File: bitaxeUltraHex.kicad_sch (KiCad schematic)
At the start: 2 parts, among them J1 Conn_01x01, J2 Conn_01x01

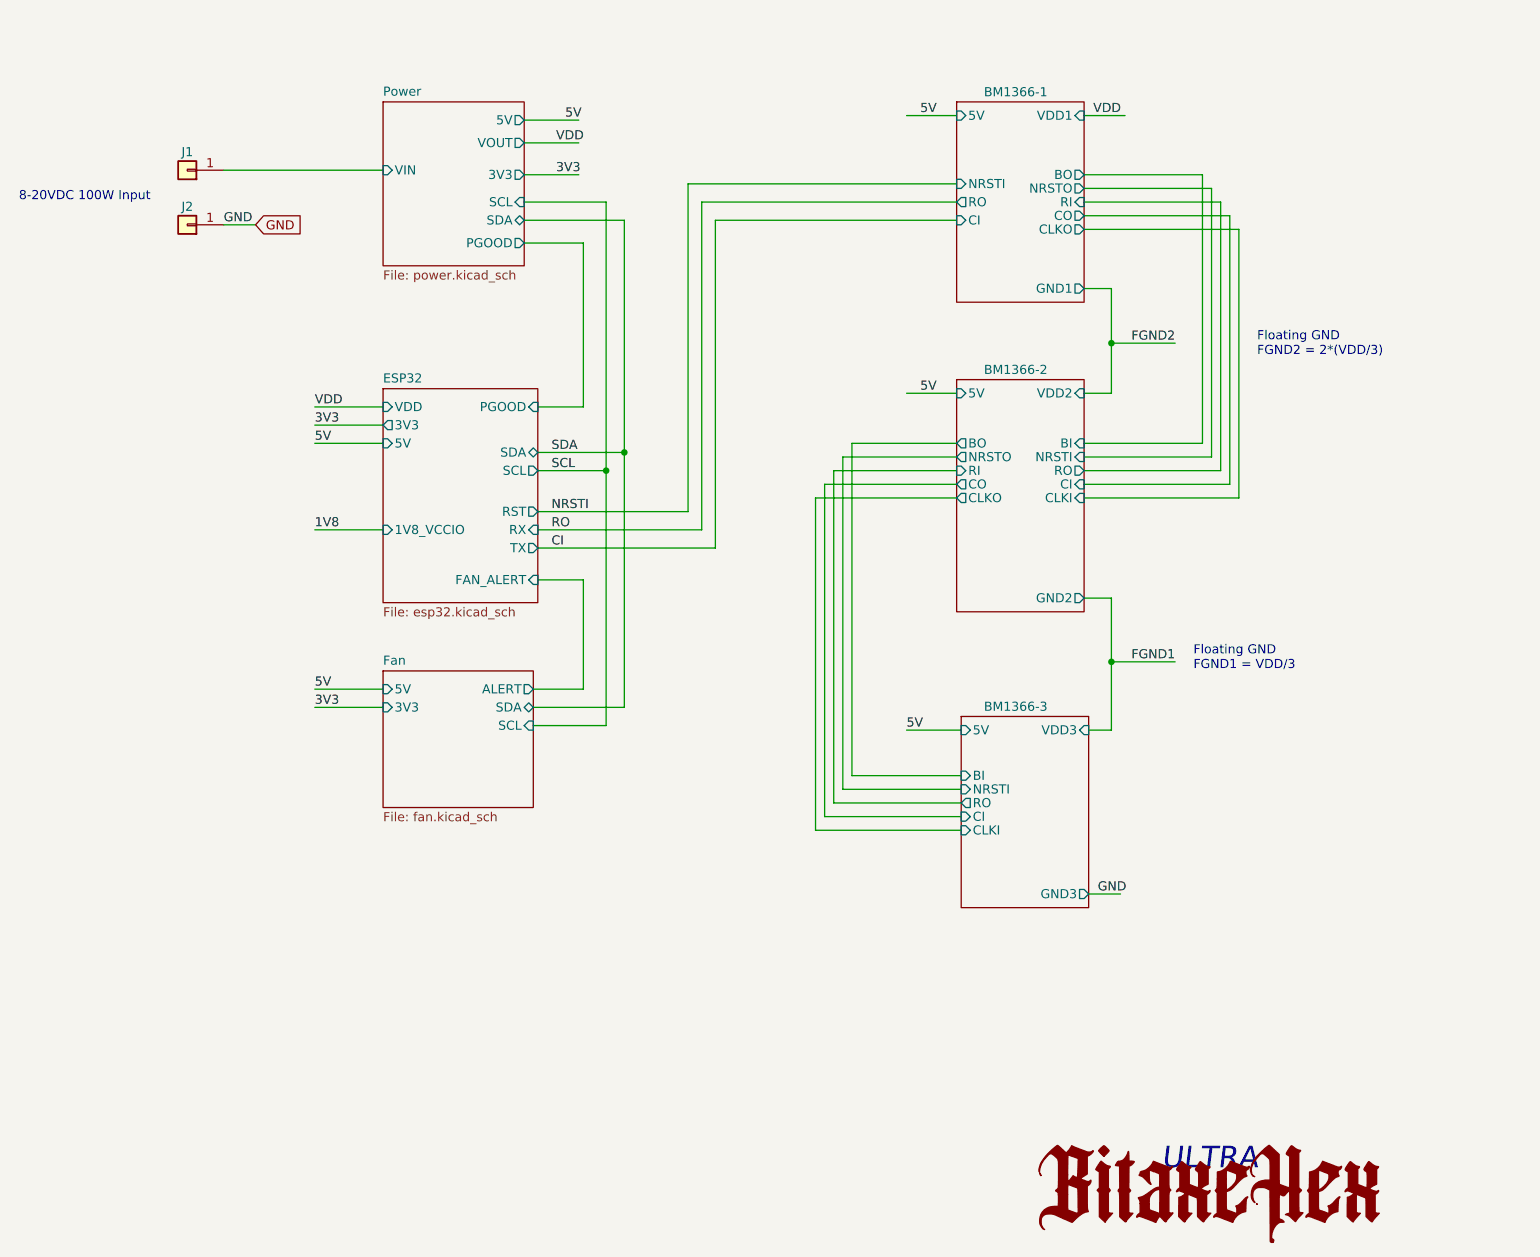
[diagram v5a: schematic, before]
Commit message: add level translator circuits to ASIC communications
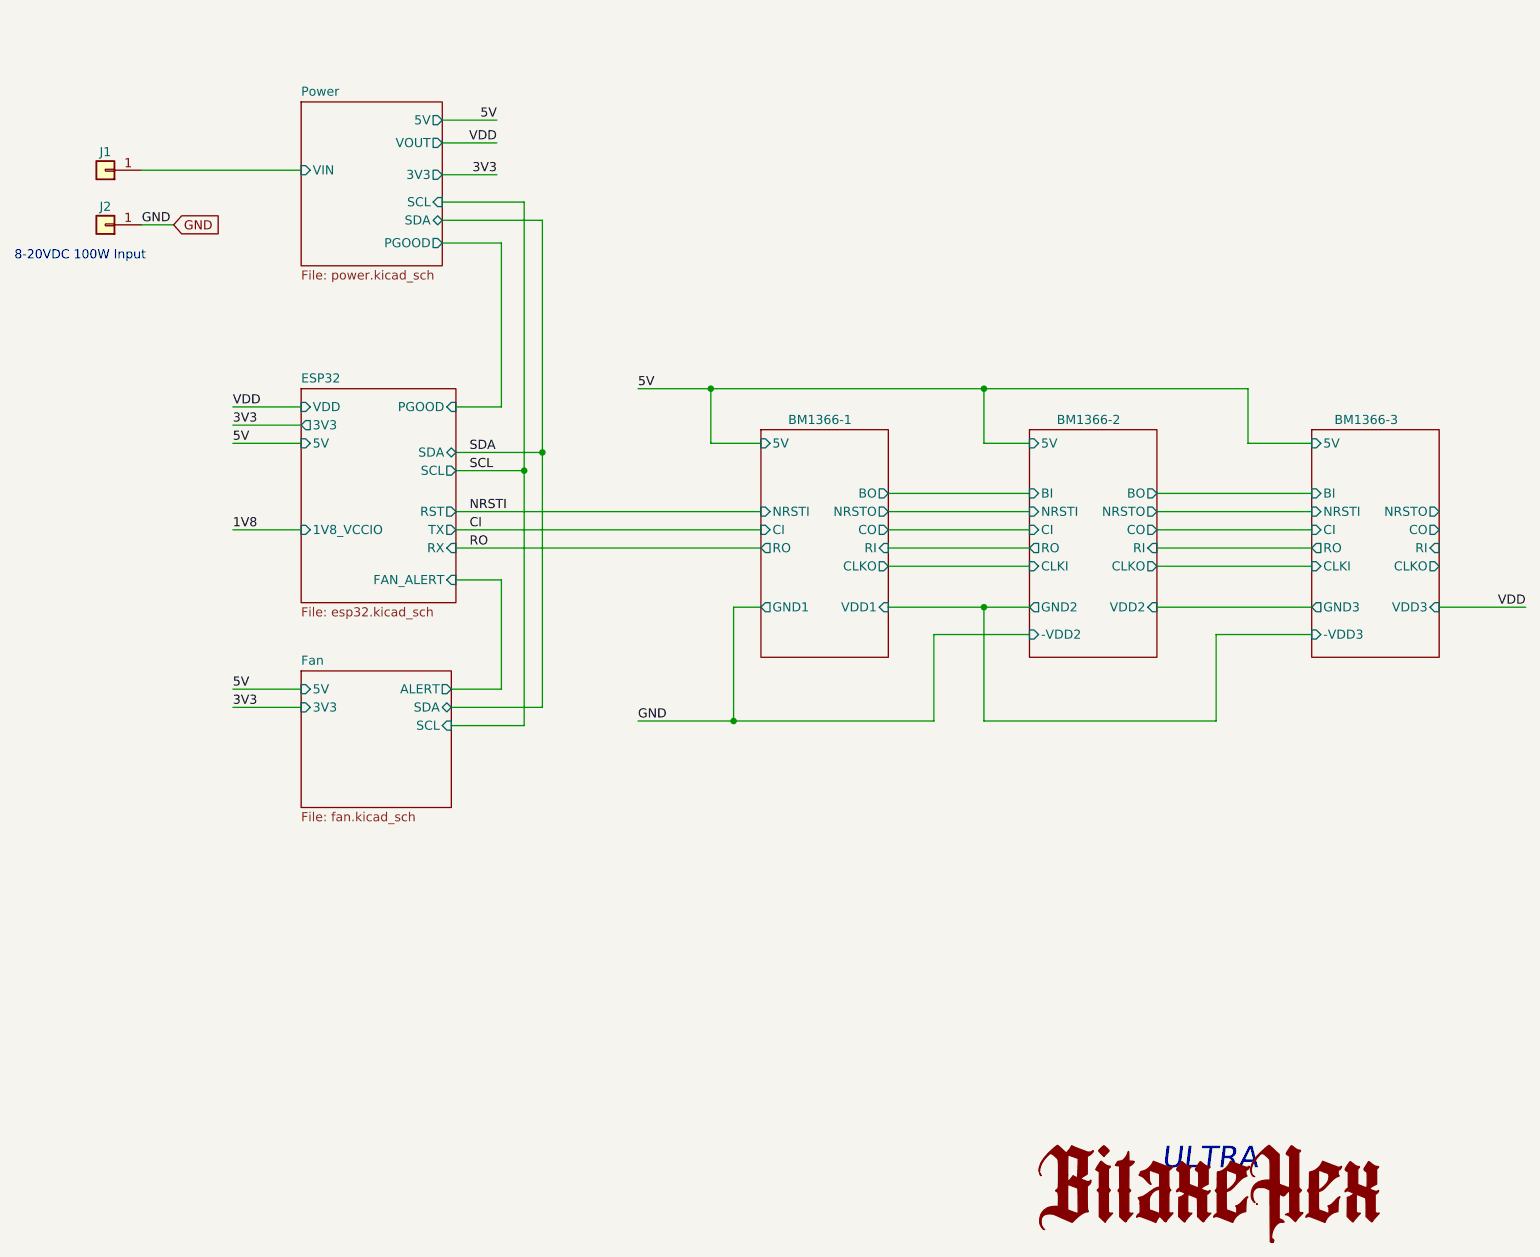
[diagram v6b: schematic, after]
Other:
- sheet BM1366-2 ports: added -VDD2; removed none
- sheet BM1366-3 ports: added -VDD3, CLKO, CO, NRSTO, RI; removed none
- note removed: "Floating GND FGND1 = VDD/3"
- note removed: "Floating GND FGND2 = 2*(VDD/3)"
- moved on the sheet: J1, J2

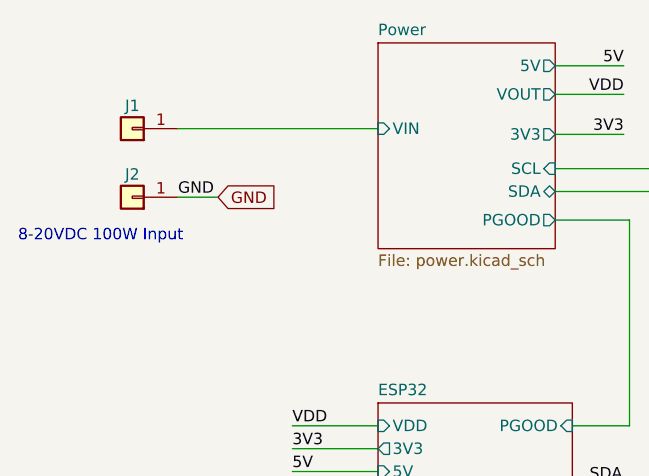
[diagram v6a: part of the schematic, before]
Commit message: Update temperature sensors, start deep review
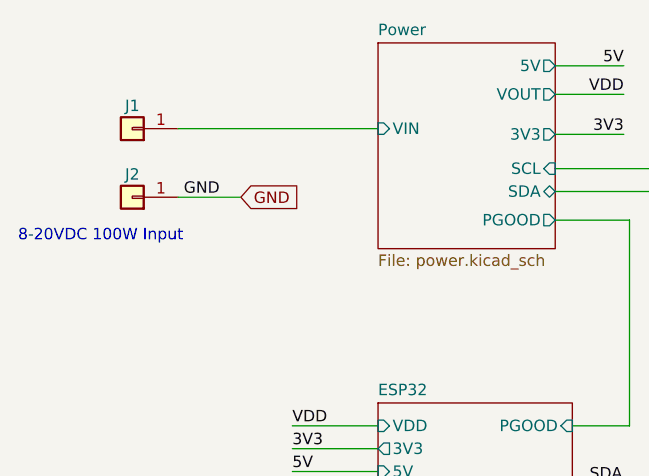
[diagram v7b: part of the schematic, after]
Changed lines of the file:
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@@
     (stroke (width 0) (type default))
   )
-  (wire (pts (xy 37.465 45.72) (xy 41.91 45.72))
+  (wire (pts (xy 37.465 45.72) (xy 44.45 45.72))
     (stroke (width 0) (type default))
   )
@@
     (effects (font (size 1.27 1.27)) (justify left bottom))
   )
-  (label "GND" (at 37.465 45.72 0) (fields_autoplaced)
+  (label "GND" (at 38.1 45.72 0) (fields_autoplaced)
     (effects (font (size 1.27 1.27)) (justify left bottom))
   )
@@
     (effects (font (size 1.27 1.27)) (justify right bottom))
   )
-  (global_label "GND" (shape input) (at 41.91 45.72 0) (fields_autoplaced)
+  (global_label "GND" (shape input) (at 44.45 45.72 0) (fields_autoplaced)
     (effects (font (size 1.27 1.27)) (justify left))
-    (property "Intersheetrefs" "${INTERSHEET_REFS}" (at 48.1936 45.6406 0)
+    (property "Intersheetrefs" "${INTERSHEET_REFS}" (at 50.7336 45.6406 0)
       (effects (font (size 1.27 1.27)) (justify left) hide)
     )

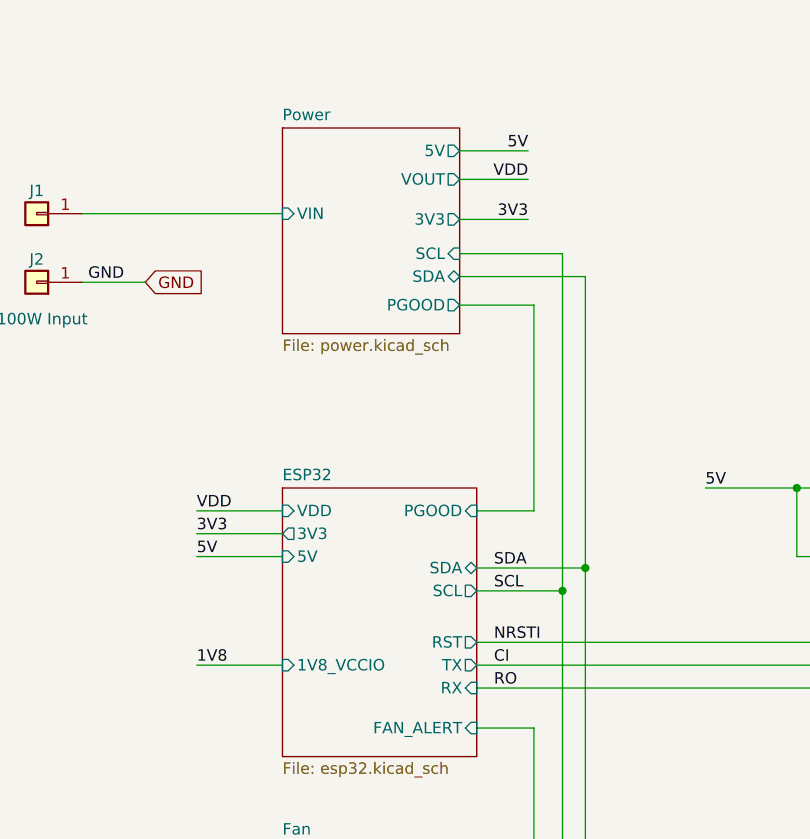
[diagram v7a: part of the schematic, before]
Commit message: add 1v8 LDO and consolidate voltage level translators
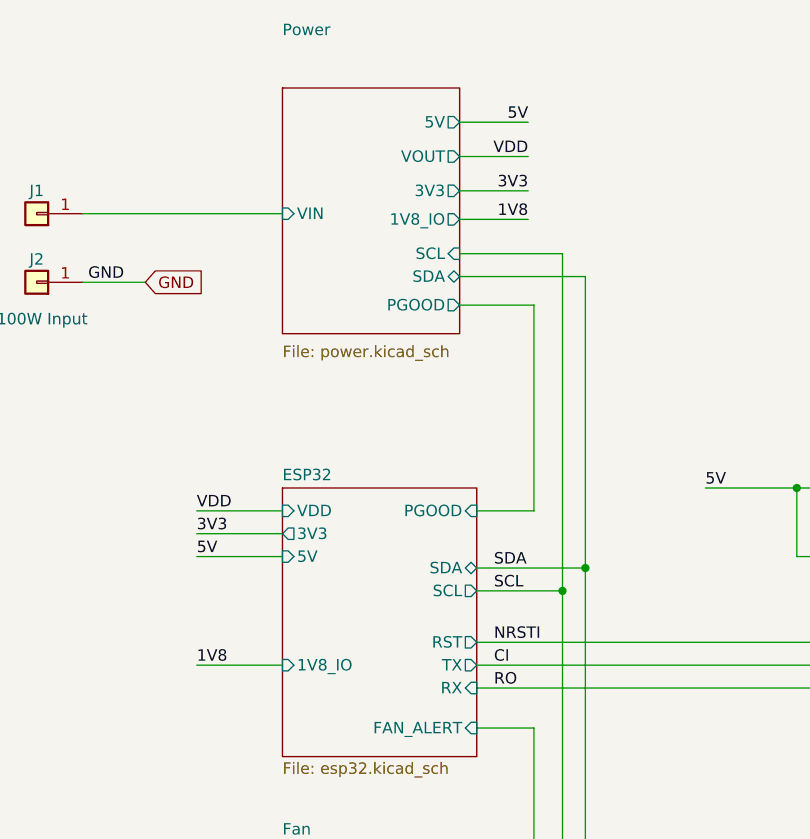
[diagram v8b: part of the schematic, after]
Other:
- sheet ESP32 ports: added 1V8_IO; removed 1V8_VCCIO
- sheet Power ports: added 1V8_IO; removed none
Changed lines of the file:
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@@
-    (stroke (width 0) (type default))
-  )
-  (wire (pts (xy 79.375 31.115) (xy 86.995 31.115))
     (stroke (width 0) (type default))
   )
@@
     (stroke (width 0) (type default))
   )
+  (wire (pts (xy 79.375 38.735) (xy 86.995 38.735))
+    (stroke (width 0) (type default))
+  )
   (wire (pts (xy 147.955 102.87) (xy 161.29 102.87))
     (stroke (width 0) (type default))
@@
     (stroke (width 0) (type default))
   )
-  (wire (pts (xy 79.375 34.29) (xy 86.995 34.29))
+  (wire (pts (xy 79.375 31.75) (xy 86.995 31.75))
     (stroke (width 0) (type default))
   )
@@
     (stroke (width 0) (type default))
   )
+  (wire (pts (xy 79.375 27.94) (xy 86.995 27.94))
+    (stroke (width 0) (type default))
+  )
   (wire (pts (xy 147.955 114.935) (xy 147.955 102.87))
     (stroke (width 0) (type default))
@@
     (stroke (width 0) (type default))
   )
-  (wire (pts (xy 79.375 38.735) (xy 86.995 38.735))
+  (wire (pts (xy 79.375 35.56) (xy 86.995 35.56))
     (stroke (width 0) (type default))
   )
@@
     (effects (font (size 1.27 1.27)) (justify left bottom))
   )
-  (label "5V" (at 86.995 31.115 180) (fields_autoplaced)
+  (label "5V" (at 86.995 27.94 180) (fields_autoplaced)
     (effects (font (size 1.27 1.27)) (justify right bottom))
   )
@@
     (effects (font (size 1.27 1.27)) (justify left bottom))
   )
-  (label "3V3" (at 86.995 38.735 180) (fields_autoplaced)
+  (label "1V8" (at 86.995 38.735 180) (fields_autoplaced)
     (effects (font (size 1.27 1.27)) (justify right bottom))
   )
+  (label "3V3" (at 86.995 35.56 180) (fields_autoplaced)
+    (effects (font (size 1.27 1.27)) (justify right bottom))
+  )
   (label "3V3" (at 50.165 73.66 0) (fields_autoplaced)
     (effects (font (size 1.27 1.27)) (justify left bottom))
@@
     (effects (font (size 1.27 1.27)) (justify left bottom))
   )
-  (label "VDD" (at 86.995 34.29 180) (fields_autoplaced)
+  (label "VDD" (at 86.995 31.75 180) (fields_autoplaced)
     (effects (font (size 1.27 1.27)) (justify right bottom))
   )
@@
     )
   )
-  (sheet (at 59.69 28.575) (size 19.685 22.86) (fields_autoplaced)
+  (sheet (at 59.69 24.13) (size 19.685 27.305)
     (stroke (width 0.1524) (type solid))
     (fill (color 255 255 194 1.0000))
-    (property "Sheetname" "Power" (at 59.69 27.8634 0)
+    (property "Sheetname" "Power" (at 59.69 18.415 0)
       (effects (font (size 1.27 1.27)) (justify left bottom))
     )
-    (property "Sheetfile" "power.kicad_sch" (at 59.69 52.0196 0)
+    (property "Sheetfile" "power.kicad_sch" (at 59.69 52.705 0)
       (effects (font (size 1.27 1.27)) (justify left top))
     )
-    (pin "VOUT" output (at 79.375 34.29 0)
+    (pin "VOUT" output (at 79.375 31.75 0)
       (effects (font (size 1.27 1.27)) (justify right))
     )
@@
       (effects (font (size 1.27 1.27)) (justify right))
     )
-    (pin "5V" output (at 79.375 31.115 0)
-      (effects (font (size 1.27 1.27)) (justify right))
-    )
-    (pin "3V3" output (at 79.375 38.735 0)
+    (pin "5V" output (at 79.375 27.94 0)
+      (effects (font (size 1.27 1.27)) (justify right))
+    )
+    (pin "3V3" output (at 79.375 35.56 0)
       (effects (font (size 1.27 1.27)) (justify right))
     )
     (pin "PGOOD" output (at 79.375 48.26 0)
+      (effects (font (size 1.27 1.27)) (justify right))
+    )
+    (pin "1V8_IO" output (at 79.375 38.735 0)
       (effects (font (size 1.27 1.27)) (justify right))
     )
@@
       (effects (font (size 1.27 1.27)) (justify right))
     )
-    (pin "1V8_VCCIO" input (at 59.69 88.265 180)
-      (effects (font (size 1.27 1.27)) (justify left))
-    )
+    (pin "1V8_IO" input (at 59.69 88.265 180)
+      (effects (font (size 1.27 1.27)) (justify left))
+    )
